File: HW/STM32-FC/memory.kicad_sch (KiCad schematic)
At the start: 2 parts, among them U5 W25X40CLSN

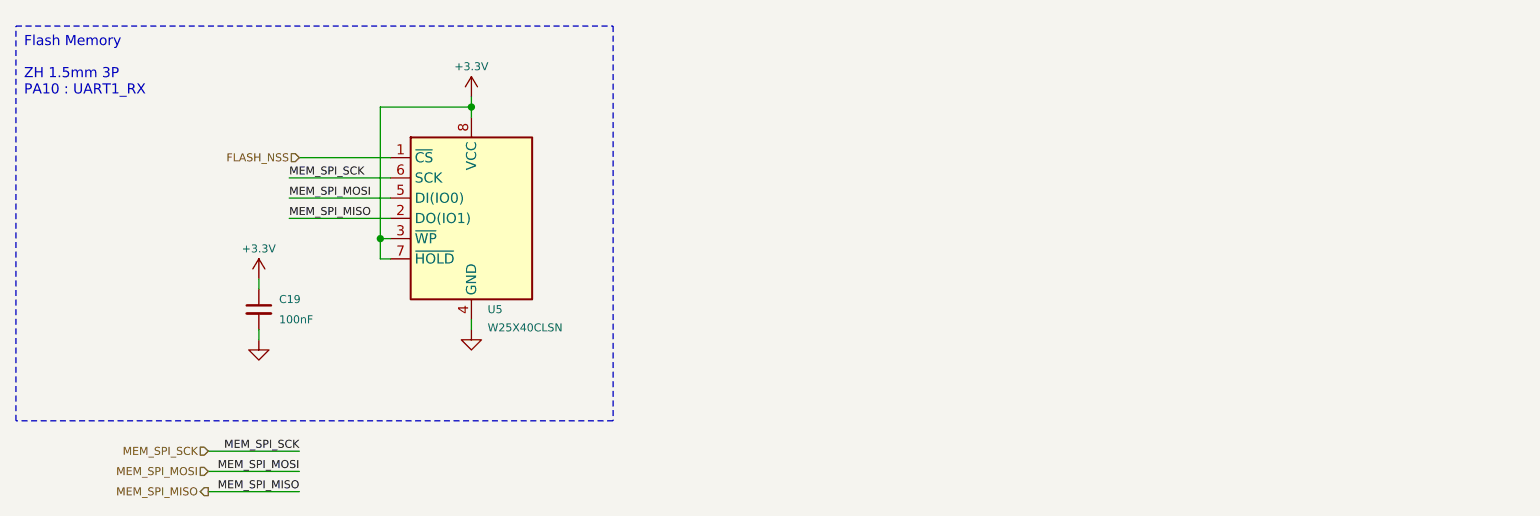
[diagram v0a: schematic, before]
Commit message: 2025.01.03v2:PM(Power Module) added
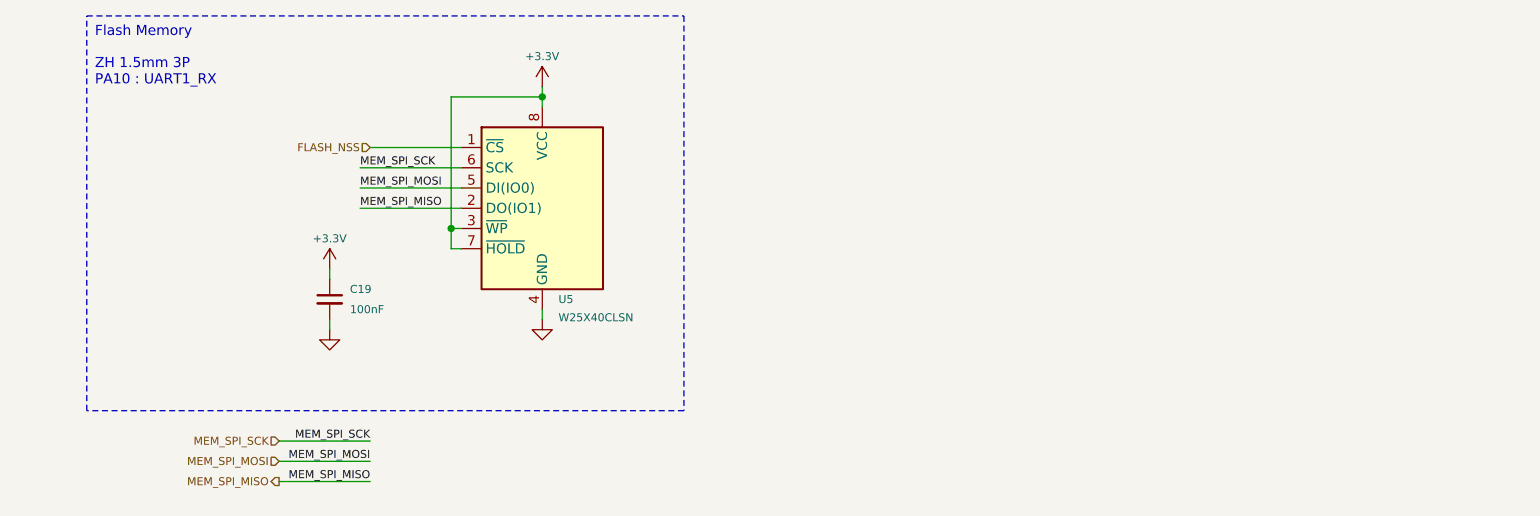
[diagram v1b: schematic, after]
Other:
- company: INHA UNIV. NARAE -> NARAE
- title: STM32 Flight Controller -> Memory
- moved on the sheet: C19, U5

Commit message: Baro/SD Card update
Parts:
- added C20: 100nF, Capacitor_SMD:C_0402_1005Metric, symbol Device:C_Small
- added J6: Micro_SD_Card_Det1, Connector_Card:microSD_HC_Molex_104031-0811, symbol Connector:Micro_SD_Card_Det1
- added R10, R11, R12, R13, R14: 10k, Resistor_SMD:R_0402_1005Metric, symbol Device:R_Small_US
- U5: footprint Package_SO:SOIC-8_3.9x4.9mm_P1.27mm -> W25X40CLUX:USON_LUXIG_TR_HandSolder; symbol Memory_Flash:W25X40CLSN -> W25X40CLUX:W25X40CLUX
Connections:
- net +3.3V: now also C20.1, J6.4 (VDD), R10.1, R11.1, R12.1, R13.1
- net GND: now also C20.2, J6.10 (SHIELD), J6.6 (VSS)
- net MEM_SPI_MISO: now also J6.7 (DAT0), R10.2
- net MEM_SPI_MOSI: now also J6.3 (CMD), R12.2
- net MEM_SPI_SCK: now also J6.5 (CLK), R11.2
- new net: J6.9 (DET), R14.2
- new net MSD_DETECT: R14.1
- new net MSD_NSS: J6.2 (DAT3/CD), R13.2
- no-connect marks 0 -> 3
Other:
- note added: "Micro SD Card"

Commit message: 2025.01.16
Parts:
- renumbered C20 to C19, C19 to C20
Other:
- note added: "PB13 : SPI2_SCK PB14 : SPI2_MISO PB15 : SPI2_MOSI PC13 : FLASH_NSS"
- note added: "PB13 : SPI2_SCK PB14 : SPI2_MISO PB15 : SPI2_MOSI PC14 : MSD_NSS PC15 : MSD_DETECT"
- note removed: "ZH 1.5mm 3P PA10 : UART1_RX"
- moved on the sheet: C19

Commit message: 2025.01.17 : PCB layout
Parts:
- U5: footprint W25X40CLUX:USON_LUXIG_TR_HandSolder -> W25X40CLUX:USON_LUXIG TR_WIN-L
- renumbered C20 to C19, C19 to C20, J6 to J4, R10 to R11, R11 to R12, R12 to R13, R13 to R14, R14 to R15

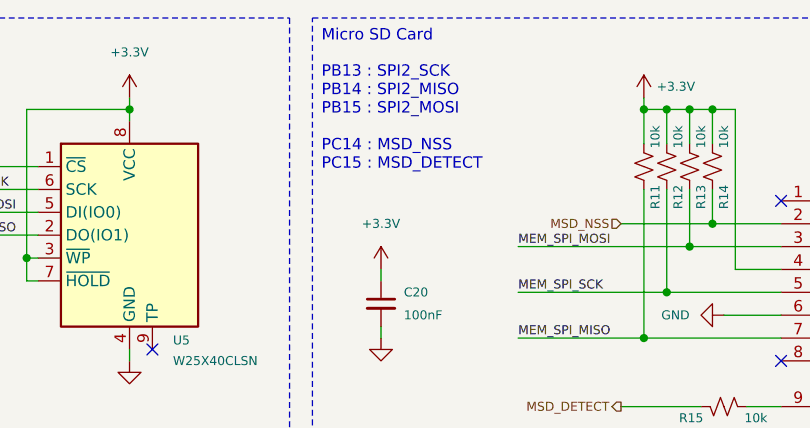
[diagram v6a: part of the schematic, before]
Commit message: 2025.02.01 PCB routing update 1
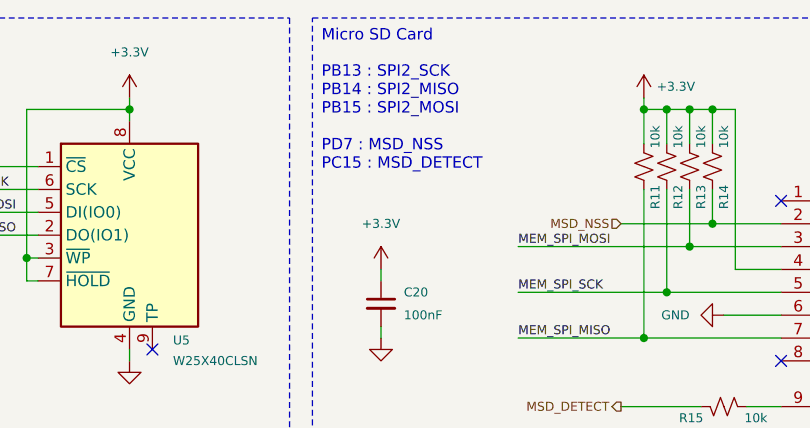
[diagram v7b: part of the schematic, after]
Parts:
- J4: footprint Connector_Card:microSD_HC_Molex_104031-0811 -> Connector_Card:microSD_HC_Hirose_DM3D-SF
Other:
- note added: "PB13 : SPI2_SCK PB14 : SPI2_MISO PB15 : SPI2_MOSI PD7 : MSD_NSS PC15 : MSD_DETECT"
- note removed: "PB13 : SPI2_SCK PB14 : SPI2_MISO PB15 : SPI2_MOSI PC14 : MSD_NSS PC15 : MSD_DETECT"
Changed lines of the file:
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@@
 		)
 	)
-	(text "PB13 : SPI2_SCK\nPB14 : SPI2_MISO\nPB15 : SPI2_MOSI\n\nPC14 : MSD_NSS\nPC15 : MSD_DETECT"
+	(text "PB13 : SPI2_SCK\nPB14 : SPI2_MISO\nPB15 : SPI2_MOSI\n\nPD7 : MSD_NSS\nPC15 : MSD_DETECT"
 		(exclude_from_sim no)
 		(at 101.346 18.034 0)
@@
 			)
 		)
-		(property "Footprint" "Connector_Card:microSD_HC_Molex_104031-0811"
+		(property "Footprint" "Connector_Card:microSD_HC_Hirose_DM3D-SF"
 			(at 227.33 25.4 0)
 			(effects
@@
 			)
 		)
-		(property "Datasheet" "https://datasheet.lcsc.com/lcsc/2110151630_XKB-Connectivity-XKTF-015-N_C381082.pdf"
+		(property "Datasheet" ""
 			(at 175.26 40.64 0)
 			(effects
